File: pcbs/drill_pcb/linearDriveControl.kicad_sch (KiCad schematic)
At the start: 15 parts, among them J301 Screw_Terminal_01x06, J302 motor1, J303 Screw_Terminal_01x03, J304 Screw_Terminal_01x03, J305 Screw_Terminal_01x06, J306 motor2, J307 TOF_senzor, J308 Screw_Terminal_01x03, J309 Screw_Terminal_01x03

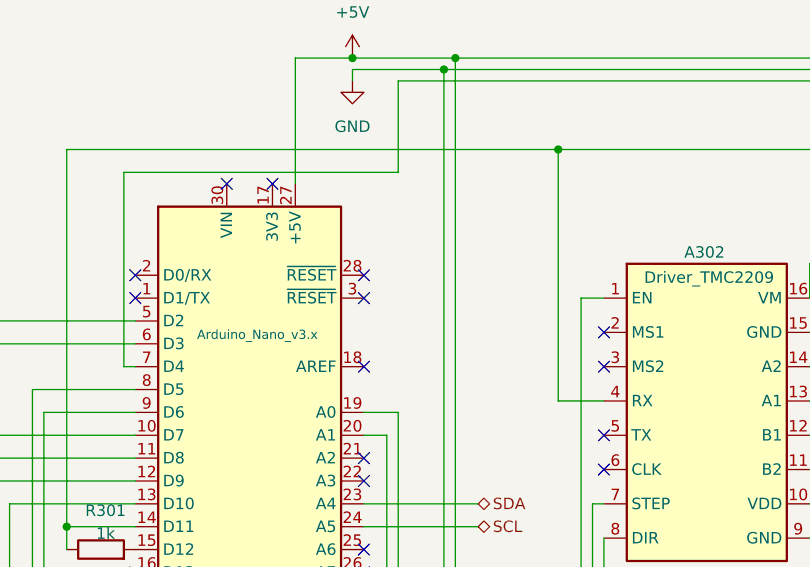
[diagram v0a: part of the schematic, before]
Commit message: added RESET connections into subsheets
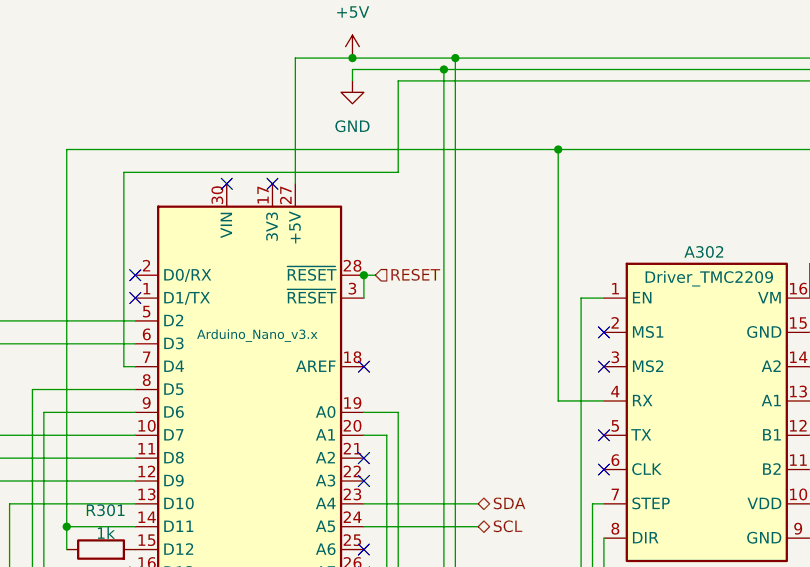
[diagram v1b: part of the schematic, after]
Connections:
- net RESET: now reaches A301.28 (~{RESET})
- net RESET: now also A301.3 (~{RESET})
- no-connect marks 20 -> 18
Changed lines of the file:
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@@
+	)
+	(junction
+		(at 92.71 71.12)
+		(diameter 0)
+		(color 0 0 0 0)
 	)
 	(junction
@@
 	)
 	(no_connect
-		(at 92.71 73.66)
-	)
-	(no_connect
 		(at 80.01 111.76)
 	)
@@
 	)
 	(no_connect
-		(at 92.71 71.12)
-	)
-	(no_connect
 		(at 82.55 60.96)
 	)
@@
 	(wire
 		(pts
+			(xy 92.71 71.12) (xy 92.71 73.66)
+		)
+		(stroke
+			(width 0)
+			(type default)
+		)
+	)
+	(wire
+		(pts
 			(xy 82.55 113.03) (xy 82.55 111.76)
 		)
@@
 	(wire
 		(pts
+			(xy 92.71 71.12) (xy 93.98 71.12)
+		)
+		(stroke
+			(width 0)
+			(type default)
+		)
+	)
+	(wire
+		(pts
 			(xy 74.93 140.97) (xy 74.93 135.89)
 		)
@@
 		)
 	)
+	(hierarchical_label "RESET"
+		(shape input)
+		(at 93.98 71.12 0)
+		(fields_autoplaced yes)
+		(effects
+			(font
+				(size 1.27 1.27)
+			)
+			(justify left)
+		)
+	)

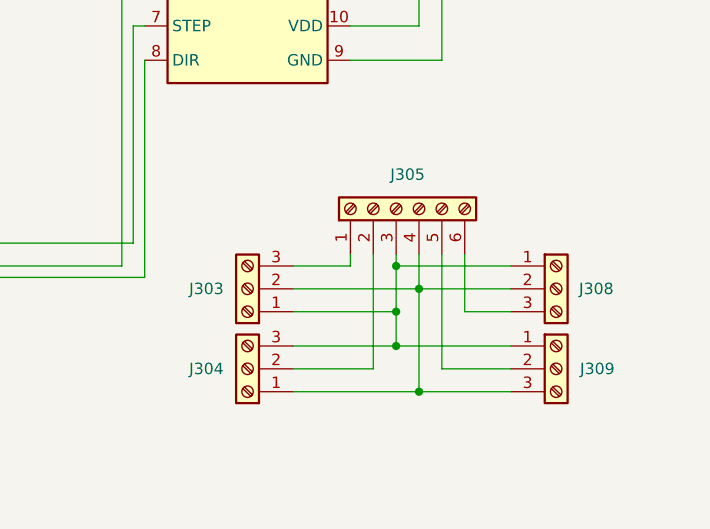
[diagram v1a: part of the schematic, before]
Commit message: Mostly finished PCB v1.0.0 Missing strain gauge control circuit
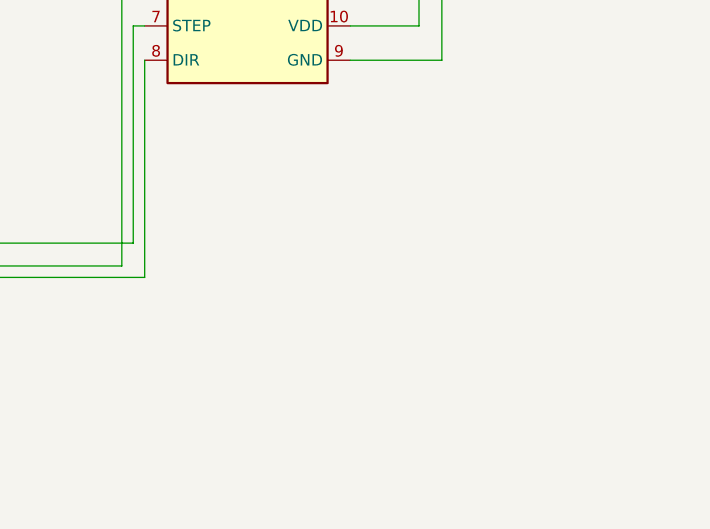
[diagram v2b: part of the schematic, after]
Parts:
- removed J303, J304, J308, J309: Screw_Terminal_01x03, Connector_JST:JST_XH_S3B-XH-A-1_1x03_P2.50mm_Horizontal, symbol Connector:Screw_Terminal_01x03
- removed J305: Screw_Terminal_01x06, Connector_JST:JST_XH_S6B-XH-A-1_1x06_P2.50mm_Horizontal, symbol Connector:Screw_Terminal_01x06

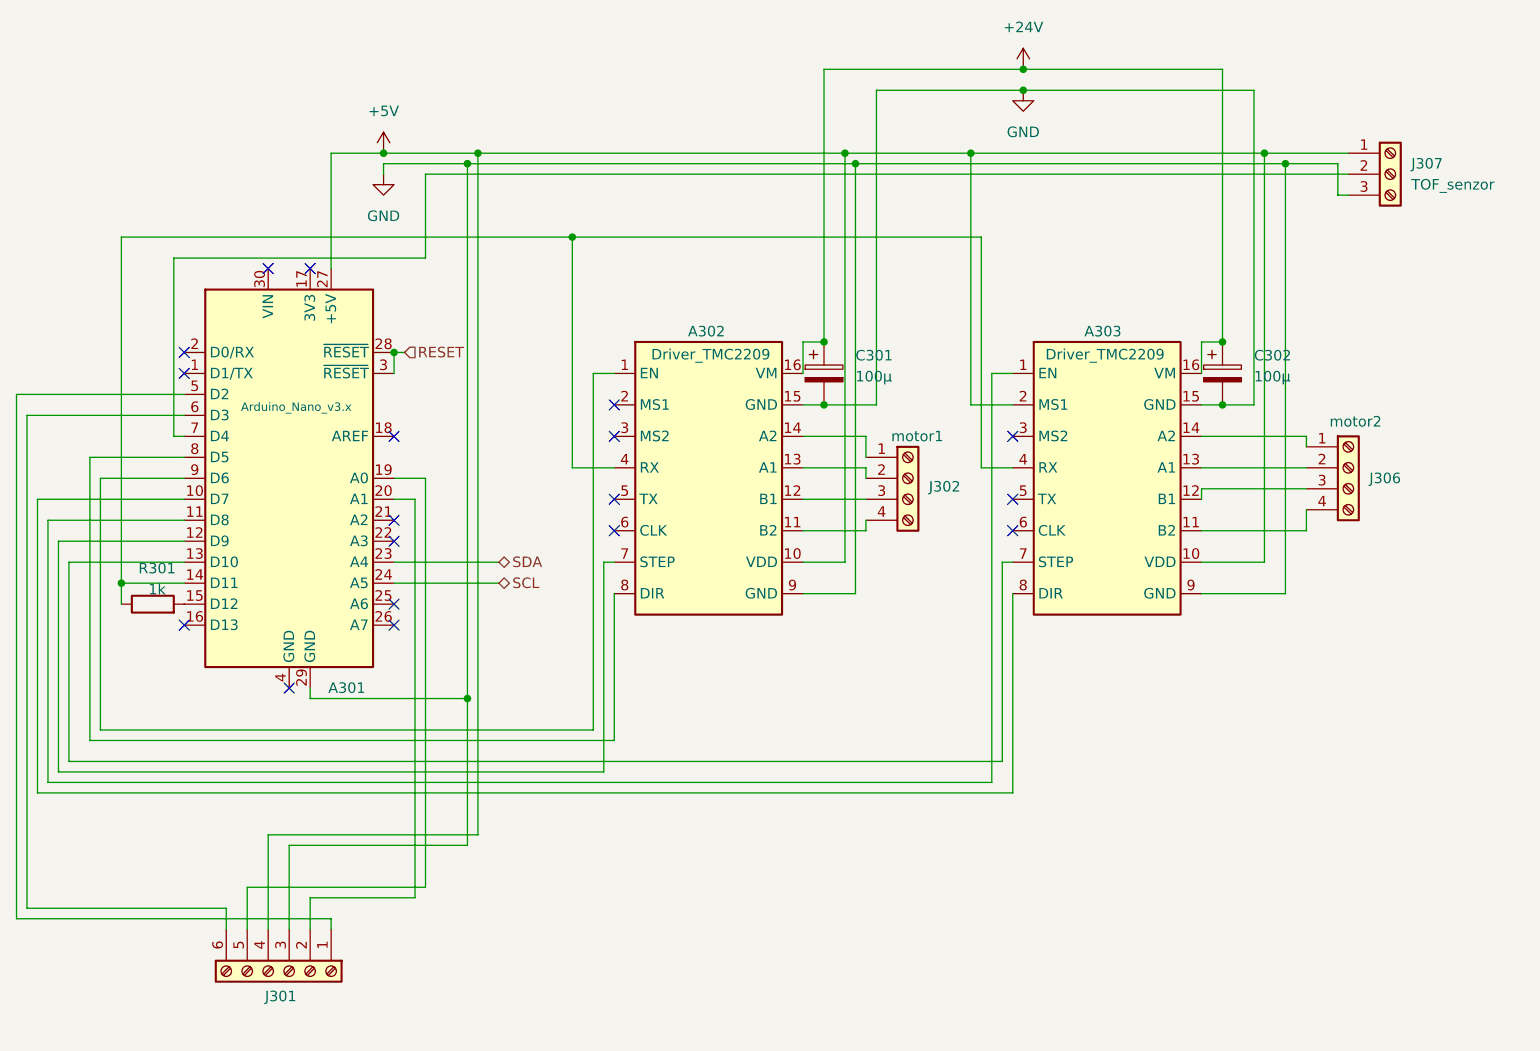
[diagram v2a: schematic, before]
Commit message: PCB update Fixed connector silkscreen. Added H-bridge capacitors.
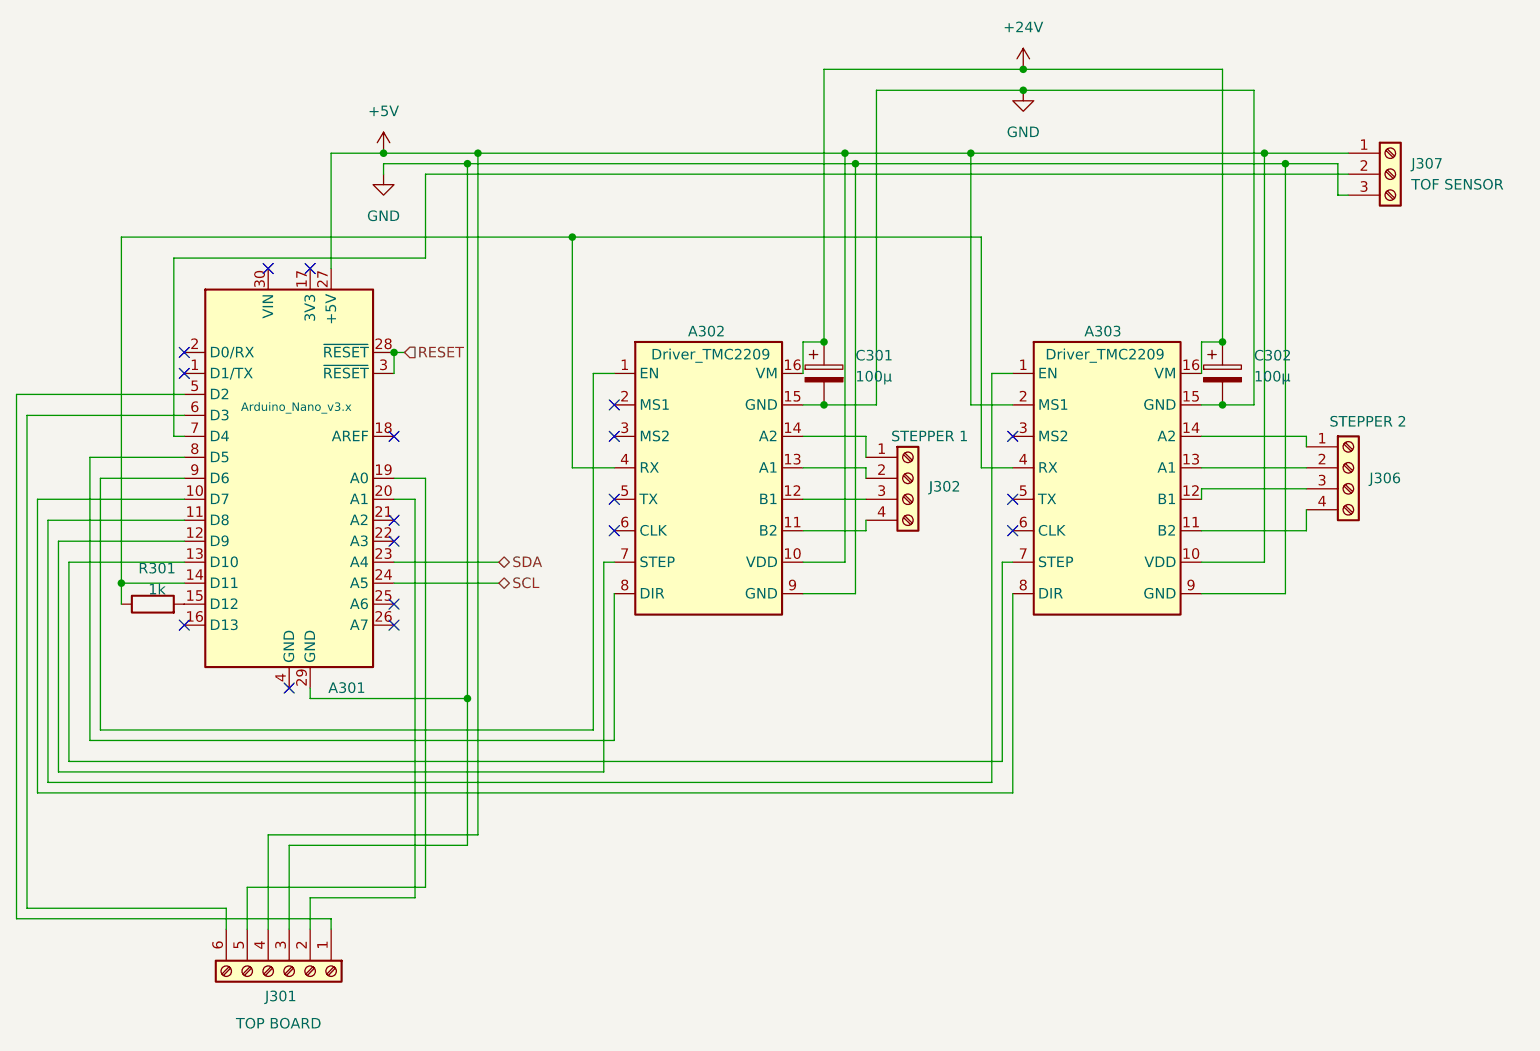
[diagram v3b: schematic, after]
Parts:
- J301: value Screw_Terminal_01x06 -> TOP BOARD
- J302: value motor1 -> STEPPER 1
- J306: value motor2 -> STEPPER 2
- J307: value TOF_senzor -> TOF SENSOR
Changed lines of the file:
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@@
 			)
 		)
-		(property "Value" "TOF_senzor"
+		(property "Value" "TOF SENSOR"
 			(at 215.9 50.7999 0)
 			(effects
@@
 			)
 		)
-		(property "Value" "Screw_Terminal_01x06"
+		(property "Value" "TOP BOARD"
 			(at 78.74 152.4 90)
 			(effects
@@
 					(size 1.27 1.27)
 				)
-				(hide yes)
 			)
 		)
@@
 			)
 		)
-		(property "Value" "motor2"
+		(property "Value" "STEPPER 2"
 			(at 205.994 79.502 0)
 			(effects
@@
 			)
 		)
-		(property "Value" "motor1"
+		(property "Value" "STEPPER 1"
 			(at 152.908 81.28 0)
 			(effects
